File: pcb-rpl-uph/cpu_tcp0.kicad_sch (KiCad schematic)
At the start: 1 part, among them U5 RPL_UPH_FCBGA1744

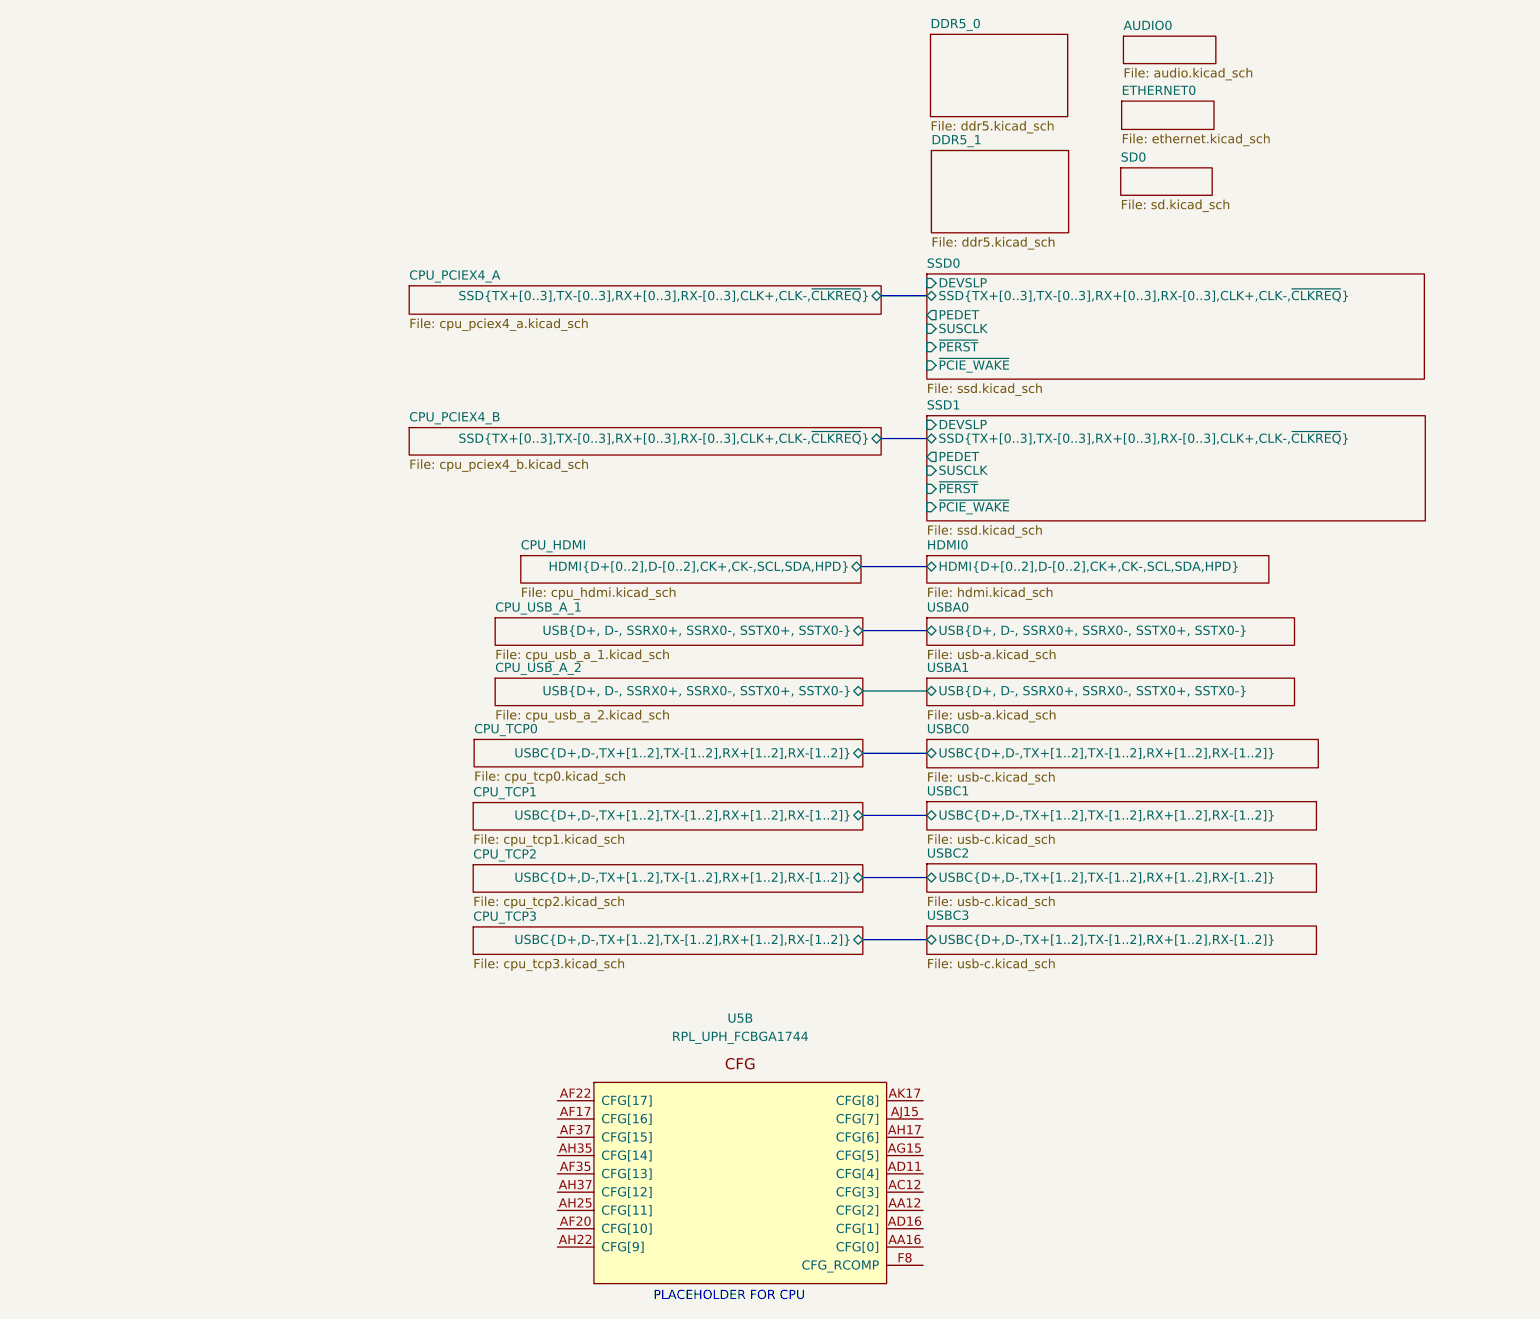
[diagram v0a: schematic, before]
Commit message: Connect USB-A and USB-C data
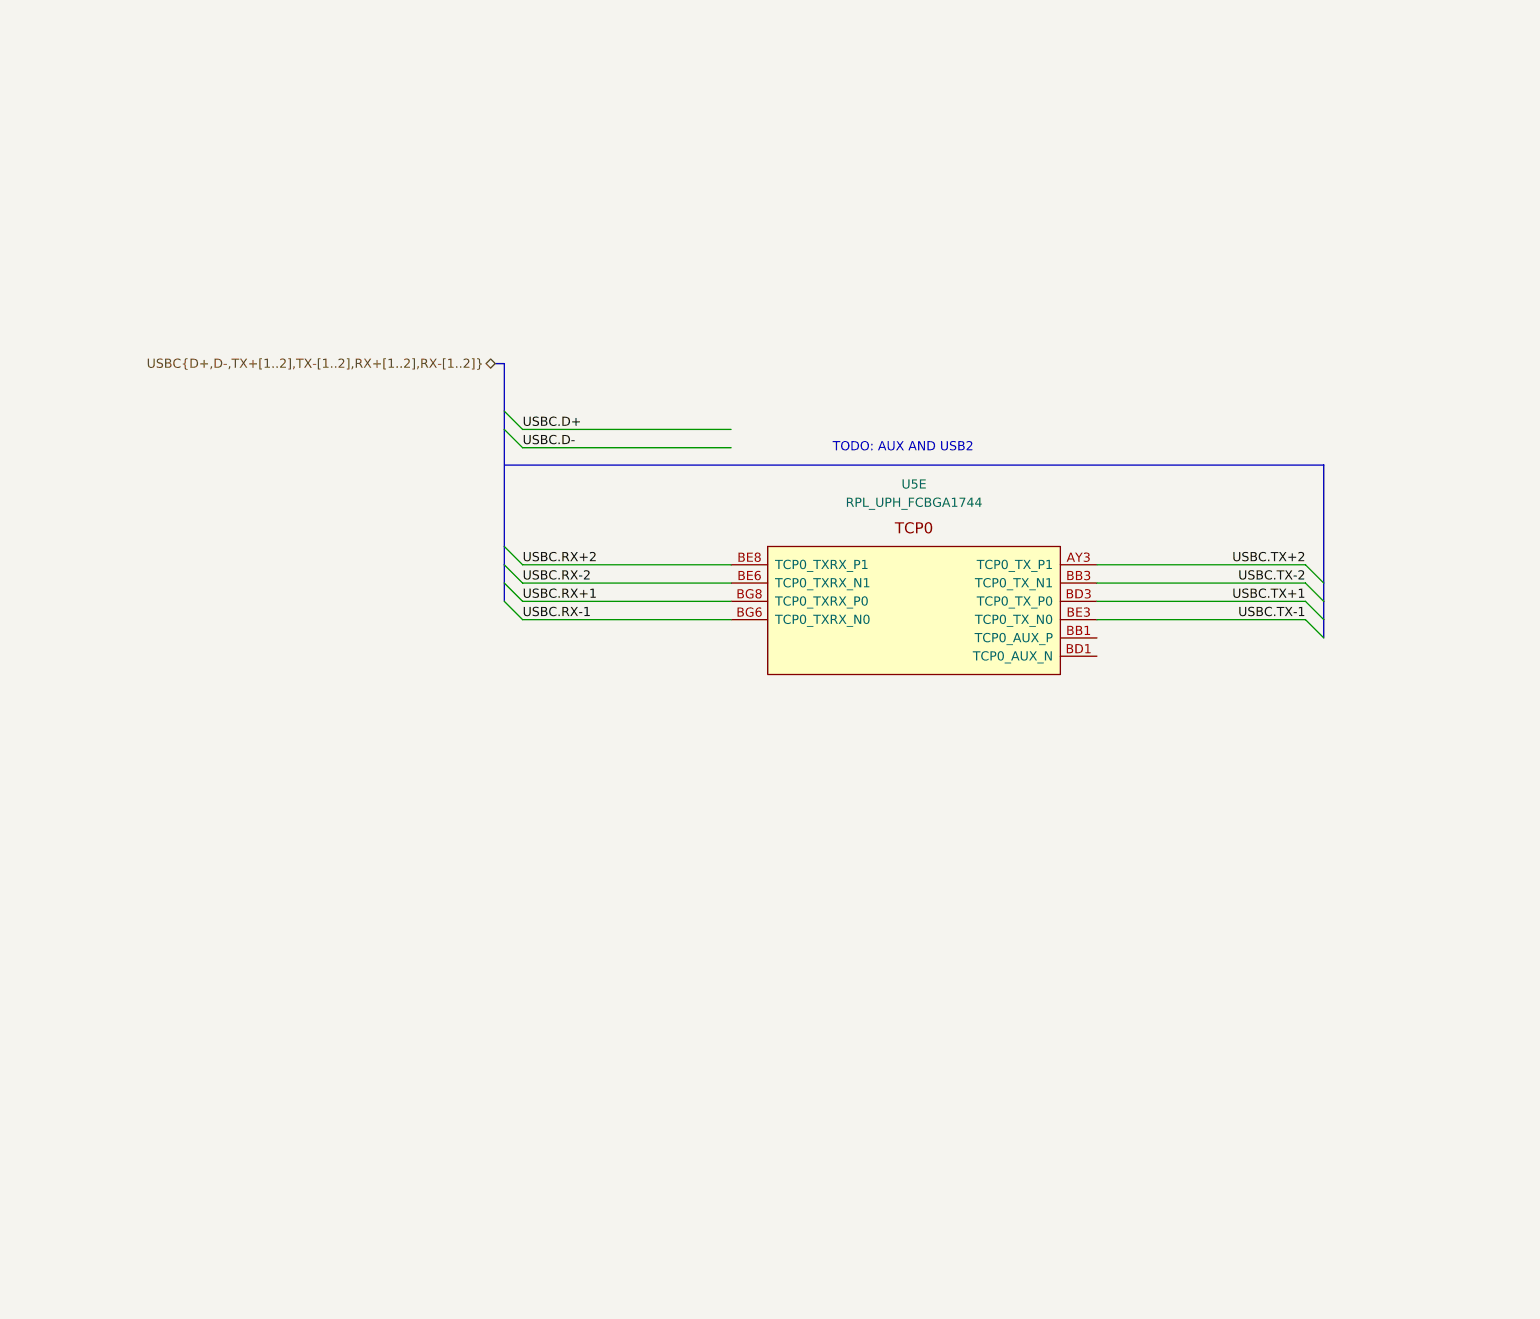
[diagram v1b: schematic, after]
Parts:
- removed U5: RPL_UPH_FCBGA1744, local:RPL_UPH_FCBGA1744, symbol local:RPL_UPH_FCBGA1744
- added U5: RPL_UPH_FCBGA1744, symbol local:RPL_UPH_FCBGA1744
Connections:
- new net USBC.RX+1: U5.BG8 (TCP0_TXRX_P0)
- new net USBC.RX+2: U5.BE8 (TCP0_TXRX_P1)
- new net USBC.RX-1: U5.BG6 (TCP0_TXRX_N0)
- new net USBC.RX-2: U5.BE6 (TCP0_TXRX_N1)
- new net USBC.TX+1: U5.BD3 (TCP0_TX_P0)
- new net USBC.TX+2: U5.AY3 (TCP0_TX_P1)
- new net USBC.TX-1: U5.BE3 (TCP0_TX_N0)
- new net USBC.TX-2: U5.BB3 (TCP0_TX_N1)
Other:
- removed sheet AUDIO0
- removed sheet CPU_HDMI
- removed sheet CPU_PCIEX4_A
- removed sheet CPU_PCIEX4_B
- removed sheet CPU_TCP0
- removed sheet CPU_TCP1
- removed sheet CPU_TCP2
- removed sheet CPU_TCP3
- removed sheet CPU_USB_A_1
- removed sheet CPU_USB_A_2
- removed sheet DDR5_0
- removed sheet DDR5_1
- removed sheet ETHERNET0
- removed sheet HDMI0
- removed sheet SD0
- removed sheet SSD0
- removed sheet SSD1
- removed sheet USBA0
- removed sheet USBA1
- removed sheet USBC0
- removed sheet USBC1
- removed sheet USBC2
- removed sheet USBC3
- note added: "TODO: AUX AND USB2"
- note removed: "PLACEHOLDER FOR CPU"

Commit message: add display connector
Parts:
- U5: footprint (none) -> local:RPL_UPH_FCBGA1744
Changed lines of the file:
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@@
       (effects (font (size 1.27 1.27)))
     )
-    (property "Footprint" "" (at 140.462 83.566 0)
+    (property "Footprint" "local:RPL_UPH_FCBGA1744" (at 140.462 83.566 0)
       (effects (font (size 1.27 1.27)) hide)
     )
